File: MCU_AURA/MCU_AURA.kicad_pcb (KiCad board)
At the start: 4 copper layers, 50 x 100 mm, 125 parts, among them J100 XT30PW-M, J101 USB_C_Receptacle_USB2.0_16P, J200 TC2050-IDC-430, J300 TF-CARD_H1.8, J400 MS621FE-FL11E, J500 Screw_Terminal_01x04, J501 TSW-108-07-G-T, J502 532617006, J504 532617004, Q300 BSS138, Q301 BSS138, Q302 BSS138, U100 TPS56C230RJER, U101 SI4825DDY-T1-GE3, U102 TPS2115ADRBR, U103 TLV62566DBVR, U104 AP2127N-1.8, U200 ESP32-S3-WROOM-1, U201 USBLC6-2SC6, U300 ICM-20948, U301 BMP280, U400 MAX-M10S, U401 RFM95W-868S2, U500 DMN6040SSD-13

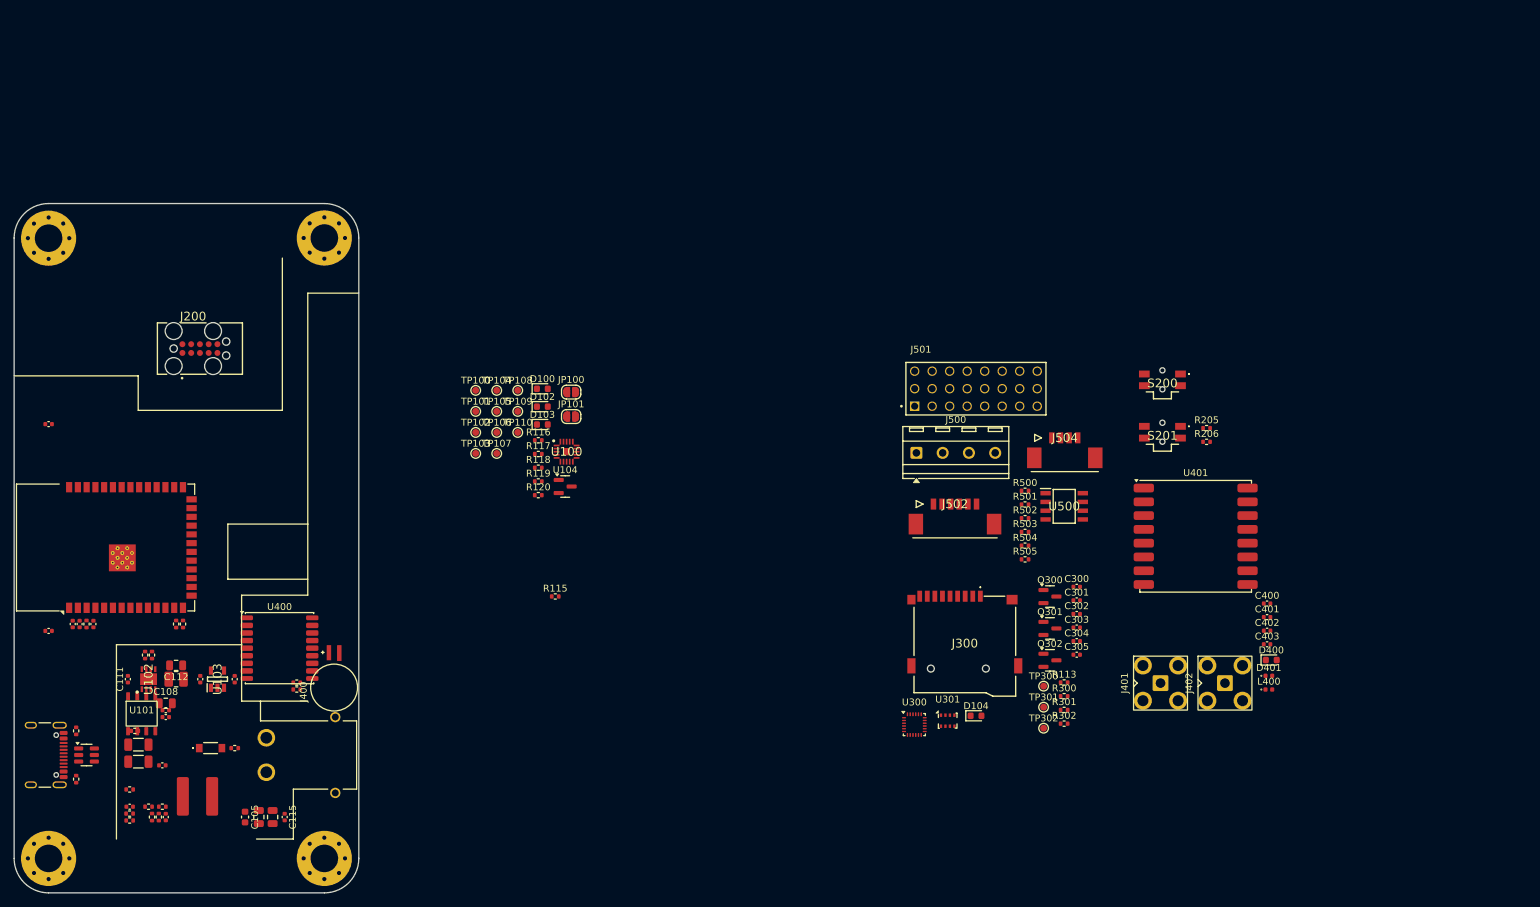
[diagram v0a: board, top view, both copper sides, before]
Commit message: Started Editing
Problem syncing desktop to laptop (libraries).
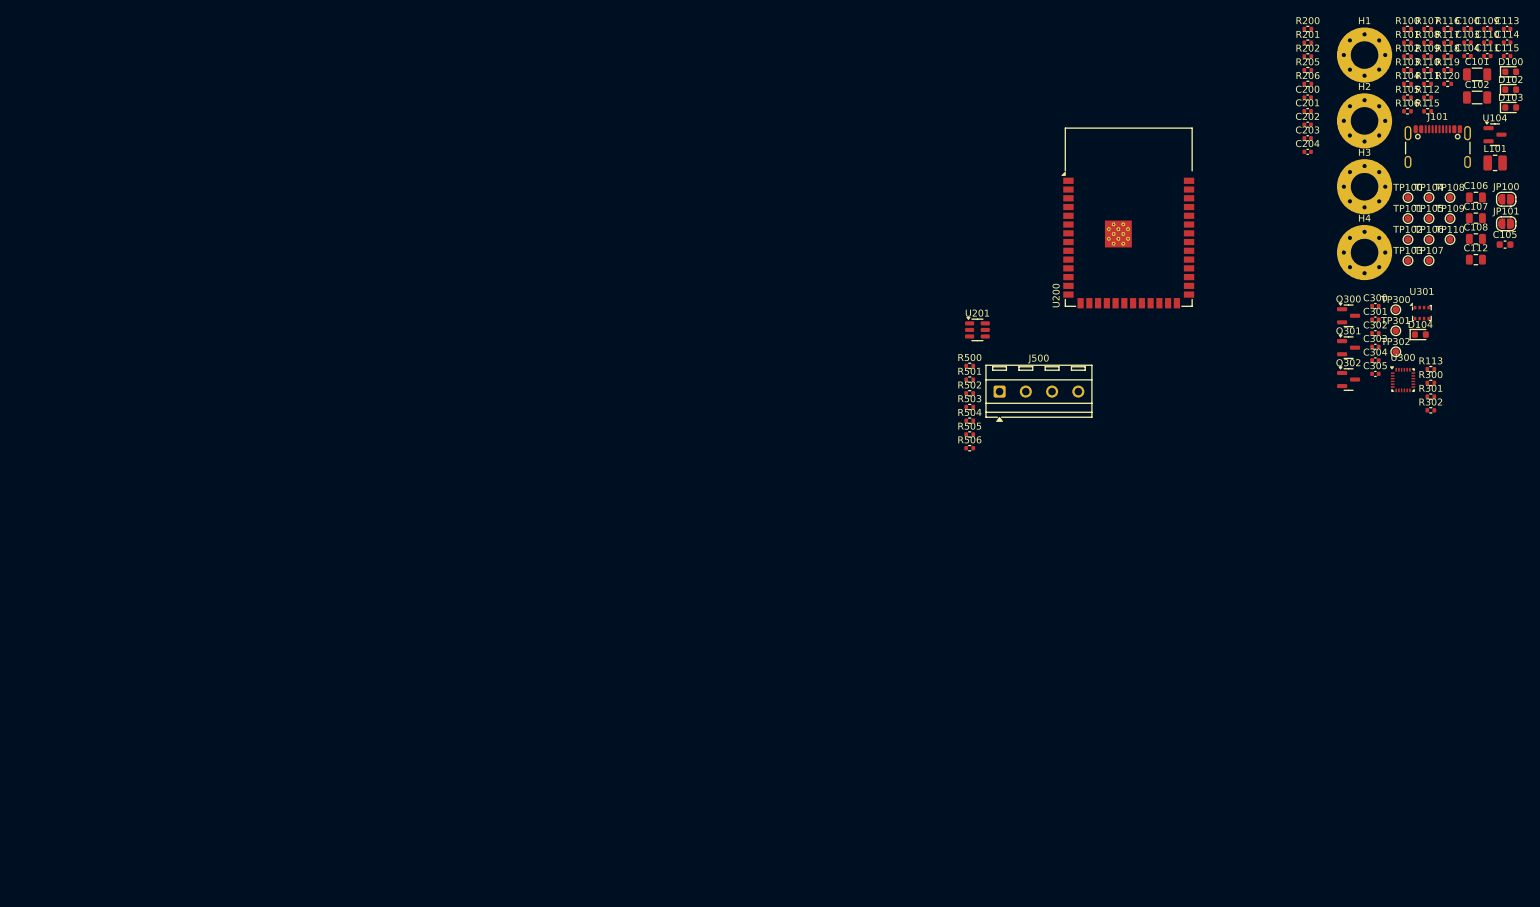
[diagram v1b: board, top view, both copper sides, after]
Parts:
- removed C400, C401, C402: 100n, Capacitor_SMD:C_0402_1005Metric
- removed C403: 10u, Capacitor_SMD:C_0402_1005Metric
- removed D101: MMSZ5242B, SamacSys_Parts:MMSZ5252B
- removed D400: LED, LED_SMD:LED_0603_1608Metric
- removed D401: ~, Diode_SMD:D_0402_1005Metric
- removed J100: XT30PW-M, SamacSys_Parts:XT30PWM
- removed J200: TC2050-IDC-430, SamacSys_Parts:TC2050-IDC
- removed J300: TF-CARD_H1.8, SamacSys_Parts:TFCARDH18
- removed J400: MS621FE-FL11E, BAT_MS621FE-FL11E:BAT_MS621FE-FL11E
- removed J401, J402: ~, SMA_Connector:SMA_Connector
- removed J501: TSW-108-07-G-T, SAMTEC_TSW-108-07-G-T:SAMTEC_TSW-108-07-G-T
- removed J502: 532617006, SamacSys_Parts:532617006
- removed J504: 532617004, SamacSys_Parts:532617004
- removed L100: 1u8, CKST0603:CKST0603-1.5uHM
- removed L400: 27nH, LED_SMD:LED_0402_1005Metric
- removed R400, R401: 1k, Resistor_SMD:R_0402_1005Metric
- removed S200, S201: EVQ-PUC02K, SamacSys_Parts:EVQPUC02K
- removed U100: TPS56C230RJER, SamacSys_Parts:QFN45P300X300X100-21N-D
- removed U101: SI4825DDY-T1-GE3, SI4825DDY-T1-GE3:SI4825DDY-T1-GE3
- removed U102: TPS2115ADRBR, SamacSys_Parts:SON65P300X300X100-9N-D
- removed U103: TLV62566DBVR, SamacSys_Parts:SOT95P280X145-5N
- removed U400: MAX-M10S, RF_GPS:ublox_MAX
- removed U401: RFM95W-868S2, RF_Module:HOPERF_RFM9XW_SMD
- removed U500: DMN6040SSD-13, SamacSys_Parts:SOIC127P600X170-8N
- added R506: 10k, Resistor_SMD:R_0402_1005Metric, F.Cu at (188.6, 85.5)
- R113: value 4k7 -> 1k
- moved C103 223.5 mm to (260.8, 26.6), turned to 0 degrees
- moved R109 222.3 mm to (255.0, 28.7), turned to 0 degrees
- moved J101 220.9 mm to (256.5, 42.9), turned to 0 degrees
- moved C100 220.8 mm to (260.8, 24.7), turned to 0 degrees
- moved R108 220.0 mm to (255.0, 26.7), turned to 0 degrees
- moved C101 218.3 mm to (262.2, 31.3), turned to 0 degrees
- moved R107 217.1 mm to (255.0, 24.7)
- moved C111 216.9 mm to (263.7, 28.6), turned to 0 degrees
- moved R101 216.5 mm to (252.1, 26.7), turned to 0 degrees
- moved C109 216.1 mm to (263.7, 24.7)
- moved R102 216.0 mm to (252.1, 28.7)
- moved C102 215.7 mm to (262.2, 34.6), turned to 0 degrees
- moved C104 215.5 mm to (260.8, 28.6)
- moved C110 214.8 mm to (263.7, 26.6)
- moved H3 214.3 mm to (245.9, 47.6)
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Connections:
- net /500_Actuation Control/GND_PY1 renamed /400_Actuation Control/GND_PY1
- net /500_Actuation Control/GND_PY2 renamed /400_Actuation Control/GND_PY2
- D104 pad 2: AUX_CS_LED -> +3V3
- R113 pad 1: GND -> AUX_CS_LED
- U200 pad 12: SCL -> SDA
- U200 pad 16: LORA_RST -> unconnected-(U200-IO46-Pad16)
- U200 pad 17: SERVO_1 -> SCL
- U200 pad 18: SERVO_2 -> CARD_DETECT
- U200 pad 19: SERVO_3 -> LORA_RST
- U200 pad 20: SERVO_4 -> LORA_CS
- U200 pad 21: SERVO_5 -> SD_CS
- U200 pad 22: SERVO_6 -> EXT_CS
- U200 pad 23: GPS_INT -> unconnected-(U200-IO21-Pad23)
- U200 pad 24: CARD_DETECT -> unconnected-(U200-IO47-Pad24)
- U200 pad 25: ICM_INT -> unconnected-(U200-IO48-Pad25)
- U200 pad 26: LORA_CS -> unconnected-(U200-IO45-Pad26)
- U200 pad 31: AUX_CS_LED -> unconnected-(U200-IO38-Pad31)
- U200 pad 32: /200_ESP32/TMS -> /200_ESP32/TCK
- U200 pad 33: /200_ESP32/TDI -> /200_ESP32/TDO
- U200 pad 34: /200_ESP32/TDO -> /200_ESP32/TDI
- U200 pad 35: /200_ESP32/TCK -> /200_ESP32/TMS
- U200 pad 36: unconnected-(U200-RXD0-Pad36) -> EXT_RX
- U200 pad 37: unconnected-(U200-TXD0-Pad37) -> EXT_TX
- U200 pad 6: SD_CS -> LED
- U200 pad 7: SDA -> unconnected-(U200-IO7-Pad7)
- U200 pad 8: SERVO_7 -> ICM_INT
- U200 pad 9: SERVO_8 -> GPS_INT
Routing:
- removed copper zone on In1.Cu, net GND
- removed copper zone on In2.Cu, net GND
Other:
- board outline removed

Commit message: Added Samacsys libraries
Made the libraries from the component search engine local.
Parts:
- removed C100, C114, C115: 1u, Capacitor_SMD:C_0402_1005Metric
- removed C101, C102: 22u, Capacitor_SMD:C_1206_3216Metric
- removed C103: 18n, Capacitor_SMD:C_0402_1005Metric
- removed C104, C109, C110, C201, C203, C204, C300, C301, C302, C303, C304, C305: 100n, Capacitor_SMD:C_0402_1005Metric
- removed C105: 100n, Capacitor_SMD:C_0603_1608Metric
- removed C106, C107, C108: 22u, Capacitor_SMD:C_0805_2012Metric
- removed C111, C113, C202: 10u, Capacitor_SMD:C_0402_1005Metric
- removed C112: 4u7, Capacitor_SMD:C_0805_2012Metric
- removed C200: 22u, Capacitor_SMD:C_0402_1005Metric
- removed D100, D102, D103, D104: LED, LED_SMD:LED_0603_1608Metric
- removed H1, H2, H3, H4: MountingHole_Pad, MountingHole:MountingHole_4mm_Pad_Via
- removed J101: USB_C_Receptacle_USB2.0_16P, Connector_USB:USB_C_Receptacle_GCT_USB4105-xx-A_16P_TopMnt_Horizontal
- removed J500: Screw_Terminal_01x04, TerminalBlock_MetzConnect:TerminalBlock_MetzConnect_Type086_RT03404HBLC_1x04_P3.81mm_Horizontal
- removed JP100, JP101: SolderJumper_2_Bridged, Jumper:SolderJumper-2_P1.3mm_Open_RoundedPad1.0x1.5mm
- removed L101: 2u2, Inductor_SMD:L_1008_2520Metric
- removed Q300, Q301, Q302: BSS138, Package_TO_SOT_SMD:SOT-23
- removed R100, R101: 5k1, Resistor_SMD:R_0402_1005Metric
- removed R102: 49k, Resistor_SMD:R_0402_1005Metric
- removed R103: 13k, Resistor_SMD:R_0402_1005Metric
- removed R104: 180k, Resistor_SMD:R_0402_1005Metric
- removed R105: 33k, Resistor_SMD:R_0402_1005Metric
- removed R106: 330k, Resistor_SMD:R_0402_1005Metric
- removed R107: 110k, Resistor_SMD:R_0402_1005Metric
- removed R108: 15k, Resistor_SMD:R_0402_1005Metric
- removed R109, R117: 4k7, Resistor_SMD:R_0402_1005Metric
- removed R110: 100k, Resistor_SMD:R_0402_1005Metric
- removed R111, R115, R500, R503: 220k, Resistor_SMD:R_0402_1005Metric
- removed R112, R501, R504: 22k, Resistor_SMD:R_0402_1005Metric
- removed R113, R120: 1k, Resistor_SMD:R_0402_1005Metric
- removed R116: 680R, Resistor_SMD:R_0402_1005Metric
- removed R118: 540k, Resistor_SMD:R_0402_1005Metric
- removed R119: 120k, Resistor_SMD:R_0402_1005Metric
- removed R200, R205, R206, R300, R301, R302, R502, R505, R506: 10k, Resistor_SMD:R_0402_1005Metric
- removed R201, R202: 27R, Resistor_SMD:R_0402_1005Metric
- removed TP100, TP101, TP102, TP103, TP104, TP105, TP106, TP107, TP108, TP109, TP110, TP300, TP301, TP302: TestPoint, TestPoint:TestPoint_Pad_D1.0mm
- removed U104: AP2127N-1.8, Package_TO_SOT_SMD:SOT-23
- removed U200: ESP32-S3-WROOM-1, RF_Module:ESP32-S3-WROOM-1
- removed U201: USBLC6-2SC6, Package_TO_SOT_SMD:SOT-23-6
- removed U300: ICM-20948, Sensor_Motion:InvenSense_QFN-24_3x3mm_P0.4mm
- removed U301: BMP280, Package_LGA:Bosch_LGA-8_2x2.5mm_P0.65mm_ClockwisePinNumbering

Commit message: Synchronised
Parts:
- added C100: 1u, Capacitor_SMD:C_0402_1005Metric, F.Cu at (131.4, 90.4)
- added C101: 22u, Capacitor_SMD:C_1206_3216Metric, F.Cu at (132.8, 97.0)
- added C102: 22u, Capacitor_SMD:C_1206_3216Metric, F.Cu at (132.8, 100.3)
- added C103: 18n, Capacitor_SMD:C_0402_1005Metric, F.Cu at (131.4, 92.4)
- added C104: 100n, Capacitor_SMD:C_0402_1005Metric, F.Cu at (131.4, 94.3)
- added C105: 100n, Capacitor_SMD:C_0603_1608Metric, F.Cu at (127.4, 100.3)
- added C106: 22u, Capacitor_SMD:C_0805_2012Metric, F.Cu at (152.5, 89.8)
- added C107: 22u, Capacitor_SMD:C_0805_2012Metric, F.Cu at (152.5, 92.8)
- added C108: 22u, Capacitor_SMD:C_0805_2012Metric, F.Cu at (152.5, 95.8)
- added C109: 100n, Capacitor_SMD:C_0402_1005Metric, F.Cu at (134.3, 90.4)
- added C110: 100n, Capacitor_SMD:C_0402_1005Metric, F.Cu at (134.3, 92.4)
- added C111: 10u, Capacitor_SMD:C_0402_1005Metric, F.Cu at (134.3, 94.3)
- added C112: 4u7, Capacitor_SMD:C_0805_2012Metric, F.Cu at (152.5, 98.8)
- added C113: 10u, Capacitor_SMD:C_0402_1005Metric, F.Cu at (137.1, 90.4)
- added C114: 1u, Capacitor_SMD:C_0402_1005Metric, F.Cu at (137.1, 92.4)
- added C115: 1u, Capacitor_SMD:C_0402_1005Metric, F.Cu at (137.1, 94.3)
- added C200: 22u, Capacitor_SMD:C_0402_1005Metric, F.Cu at (97.2, 104.1)
- added C201: 100n, Capacitor_SMD:C_0402_1005Metric, F.Cu at (97.2, 106.0)
- added C202: 10u, Capacitor_SMD:C_0402_1005Metric, F.Cu at (97.2, 108.0)
- added C203: 100n, Capacitor_SMD:C_0402_1005Metric, F.Cu at (97.2, 110.0)
- added C204: 100n, Capacitor_SMD:C_0402_1005Metric, F.Cu at (97.2, 112.0)
- added C300: 100n, Capacitor_SMD:C_0402_1005Metric, F.Cu at (95.5, 121.3)
- added C301: 100n, Capacitor_SMD:C_0402_1005Metric, F.Cu at (95.5, 123.2)
- added C302: 100n, Capacitor_SMD:C_0402_1005Metric, F.Cu at (95.5, 125.2)
- added C303: 100n, Capacitor_SMD:C_0402_1005Metric, F.Cu at (95.5, 127.2)
- added C304: 100n, Capacitor_SMD:C_0402_1005Metric, F.Cu at (95.5, 129.2)
- added C305: 100n, Capacitor_SMD:C_0402_1005Metric, F.Cu at (95.5, 131.1)
- added D100: LED, LED_SMD:LED_0603_1608Metric, F.Cu at (137.7, 96.6)
- added D101: MMSZ5242B, MMSZ5252B:MMSZ5252B, F.Cu at (156.5, 80.7)
- added D102: LED, LED_SMD:LED_0603_1608Metric, F.Cu at (137.7, 99.2)
- added D103: LED, LED_SMD:LED_0603_1608Metric, F.Cu at (137.7, 101.8)
- added D104: LED, LED_SMD:LED_0603_1608Metric, F.Cu at (80.9, 140.0)
- added H1: MountingHole_Pad, MountingHole:MountingHole_4mm_Pad_Via, F.Cu at (125.2, 65.6)
- added H2: MountingHole_Pad, MountingHole:MountingHole_4mm_Pad_Via, F.Cu at (125.2, 75.2)
- added H3: MountingHole_Pad, MountingHole:MountingHole_4mm_Pad_Via, F.Cu at (125.2, 84.7)
- added H4: MountingHole_Pad, MountingHole:MountingHole_4mm_Pad_Via, F.Cu at (125.2, 94.3)
- added J100: XT30PW-M, XT30PWM:XT30PWM, F.Cu at (137.8, 69.6)
- added J101: USB_C_Receptacle_USB2.0_16P, Connector_USB:USB_C_Receptacle_GCT_USB4105-xx-A_16P_TopMnt_Horizontal, F.Cu at (147.0, 83.6)
- added J200: TC2050-IDC-430, TC2050-IDC:TC2050-IDC, F.Cu at (85.1, 104.9)
- added J300: TF-CARD_H1.8, TF-CARD_H1_8:TFCARDH18, F.Cu at (79.3, 129.9)
- added J500: Screw_Terminal_01x04, TerminalBlock_MetzConnect:TerminalBlock_MetzConnect_Type086_RT03404HBLC_1x04_P3.81mm_Horizontal, F.Cu at (137.7, 109.8)
- added J502: 532617006, 532617006:532617006, F.Cu at (143.3, 117.2)
- added J504: 532617004, 532617004:532617004, F.Cu at (127.6, 107.6)
- added J505: 532617004, 532617004:532617004, F.Cu at (127.6, 116.9)
- added JP100: SolderJumper_2_Bridged, Jumper:SolderJumper-2_P1.3mm_Open_RoundedPad1.0x1.5mm, F.Cu at (156.5, 62.6)
- added JP101: SolderJumper_2_Bridged, Jumper:SolderJumper-2_P1.3mm_Open_RoundedPad1.0x1.5mm, F.Cu at (156.5, 66.2)
- added L100: 1u8, CKST0603:CKST0603-1.5uHM, F.Cu at (132.5, 83.9)
- added L101: 2u2, Inductor_SMD:L_1008_2520Metric, F.Cu at (122.9, 100.9)
- added Q300: BSS138, Package_TO_SOT_SMD:SOT-23, F.Cu at (91.6, 122.7)
- added Q301: BSS138, Package_TO_SOT_SMD:SOT-23, F.Cu at (91.6, 127.3)
- added Q302: BSS138, Package_TO_SOT_SMD:SOT-23, F.Cu at (91.6, 131.9)
- added R100: 5k1, Resistor_SMD:R_0402_1005Metric, F.Cu at (147.0, 61.8)
- added R101: 5k1, Resistor_SMD:R_0402_1005Metric, F.Cu at (147.0, 63.8)
- added R102: 49k, Resistor_SMD:R_0402_1005Metric, F.Cu at (147.0, 65.8)
- added R103: 13k, Resistor_SMD:R_0402_1005Metric, F.Cu at (147.0, 67.8)
- added R104: 180k, Resistor_SMD:R_0402_1005Metric, F.Cu at (147.0, 69.8)
- added R105: 33k, Resistor_SMD:R_0402_1005Metric, F.Cu at (147.0, 71.8)
- added R106: 330k, Resistor_SMD:R_0402_1005Metric, F.Cu at (147.0, 73.8)
- added R107: 110k, Resistor_SMD:R_0402_1005Metric, F.Cu at (149.9, 61.8)
- added R108: 15k, Resistor_SMD:R_0402_1005Metric, F.Cu at (149.9, 63.8)
- added R109: 4k7, Resistor_SMD:R_0402_1005Metric, F.Cu at (149.9, 65.8)
- added R110: 100k, Resistor_SMD:R_0402_1005Metric, F.Cu at (149.9, 67.8)
- added R111: 220k, Resistor_SMD:R_0402_1005Metric, F.Cu at (149.9, 69.8)
- added R112: 22k, Resistor_SMD:R_0402_1005Metric, F.Cu at (149.9, 71.8)
- added R113: 1k, Resistor_SMD:R_0402_1005Metric, F.Cu at (93.7, 135.2)
- added R115: 220k, Resistor_SMD:R_0402_1005Metric, F.Cu at (149.9, 73.8)
- added R116: 680R, Resistor_SMD:R_0402_1005Metric, F.Cu at (152.8, 61.8)
- added R117: 4k7, Resistor_SMD:R_0402_1005Metric, F.Cu at (152.8, 63.8)
- added R118: 540k, Resistor_SMD:R_0402_1005Metric, F.Cu at (152.8, 65.8)
- added R119: 120k, Resistor_SMD:R_0402_1005Metric, F.Cu at (152.8, 67.8)
- added R120: 1k, Resistor_SMD:R_0402_1005Metric, F.Cu at (152.8, 69.8)
- added R200: 10k, Resistor_SMD:R_0402_1005Metric, F.Cu at (94.3, 104.1)
- added R201: 27R, Resistor_SMD:R_0402_1005Metric, F.Cu at (94.3, 106.1)
- added R202: 27R, Resistor_SMD:R_0402_1005Metric, F.Cu at (94.3, 108.1)
- added R205: 10k, Resistor_SMD:R_0402_1005Metric, F.Cu at (94.3, 110.1)
- added R206: 10k, Resistor_SMD:R_0402_1005Metric, F.Cu at (94.3, 112.0)
- added R300: 10k, Resistor_SMD:R_0402_1005Metric, F.Cu at (93.7, 137.1)
- added R301: 10k, Resistor_SMD:R_0402_1005Metric, F.Cu at (93.7, 139.1)
- added R302: 10k, Resistor_SMD:R_0402_1005Metric, F.Cu at (93.7, 141.1)
- added R500: 220k, Resistor_SMD:R_0402_1005Metric, F.Cu at (121.9, 124.6)
- added R501: 22k, Resistor_SMD:R_0402_1005Metric, F.Cu at (121.9, 126.5)
- added R502: 10k, Resistor_SMD:R_0402_1005Metric, F.Cu at (121.9, 128.5)
- added R503: 220k, Resistor_SMD:R_0402_1005Metric, F.Cu at (121.9, 130.5)
- added R504: 22k, Resistor_SMD:R_0402_1005Metric, F.Cu at (121.9, 132.5)
- added R505: 10k, Resistor_SMD:R_0402_1005Metric, F.Cu at (121.9, 134.5)
- added R506: 10k, Resistor_SMD:R_0402_1005Metric, F.Cu at (121.9, 136.5)
- added S200: EVQ-PUC02K, EVQ-PUC02k:EVQPUC02K, F.Cu at (74.3, 106.4)
- added S201: EVQ-PUC02K, EVQ-PUC02k:EVQPUC02K, F.Cu at (74.3, 114.0)
- added TP100: TestPoint, TestPoint:TestPoint_Pad_D1.0mm, F.Cu at (142.6, 89.8)
- added TP101: TestPoint, TestPoint:TestPoint_Pad_D1.0mm, F.Cu at (142.6, 92.9)
- added TP102: TestPoint, TestPoint:TestPoint_Pad_D1.0mm, F.Cu at (142.6, 95.9)
- added TP103: TestPoint, TestPoint:TestPoint_Pad_D1.0mm, F.Cu at (142.6, 99.0)
- added TP104: TestPoint, TestPoint:TestPoint_Pad_D1.0mm, F.Cu at (145.7, 89.8)
- added TP105: TestPoint, TestPoint:TestPoint_Pad_D1.0mm, F.Cu at (145.7, 92.9)
- added TP106: TestPoint, TestPoint:TestPoint_Pad_D1.0mm, F.Cu at (145.7, 95.9)
- added TP107: TestPoint, TestPoint:TestPoint_Pad_D1.0mm, F.Cu at (145.7, 99.0)
- added TP108: TestPoint, TestPoint:TestPoint_Pad_D1.0mm, F.Cu at (148.7, 89.8)
- added TP109: TestPoint, TestPoint:TestPoint_Pad_D1.0mm, F.Cu at (148.7, 92.9)
- added TP110: TestPoint, TestPoint:TestPoint_Pad_D1.0mm, F.Cu at (148.7, 95.9)
- added TP300: TestPoint, TestPoint:TestPoint_Pad_D1.0mm, F.Cu at (90.7, 135.7)
- added TP301: TestPoint, TestPoint:TestPoint_Pad_D1.0mm, F.Cu at (90.7, 138.7)
- added TP302: TestPoint, TestPoint:TestPoint_Pad_D1.0mm, F.Cu at (90.7, 141.8)
- added U100: TPS56C230RJER, TPS56C230RJER:QFN45P300X300X100-21N-D, F.Cu at (157.0, 70.6)
- added U101: SI4825DDY-T1-GE3, SI4825DDY-T1-GE3:SI4825DDY-T1-GE3, F.Cu at (158.0, 92.4)
- added U102: TPS2115ADRBR, TPS2115ADRBR:SON65P300X300X100-9N-D, F.Cu at (157.0, 75.6)
- added U103: TLV62566DBVR, TLV62566DBVR:SOT95P280X145-5N, F.Cu at (155.4, 85.3)
- added U104: AP2127N-1.8, Package_TO_SOT_SMD:SOT-23, F.Cu at (157.2, 98.9)
- added U200: ESP32-S3-WROOM-1, RF_Module:ESP32-S3-WROOM-1, F.Cu at (93.9, 89.1)
- added U201: USBLC6-2SC6, Package_TO_SOT_SMD:SOT-23-6, F.Cu at (101.2, 105.5)
- added U300: ICM-20948, Sensor_Motion:InvenSense_QFN-24_3x3mm_P0.4mm, F.Cu at (71.9, 141.3)
- added U301: BMP280, Package_LGA:Bosch_LGA-8_2x2.5mm_P0.65mm_ClockwisePinNumbering, F.Cu at (76.8, 140.7)
- added U500: DMN6040SSD-13, DMN6040SSD-13:SOIC127P600X170-8N, F.Cu at (127.6, 126.8)
